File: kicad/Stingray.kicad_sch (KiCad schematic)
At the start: 51 parts, among them J1 Raspberry_Pi_5, J10 USB_A, J11 Screw_Terminal_01x10, J14 Conn_01x04_Pin, J15 USB_A, J16 USB_A, J17 USB_A, J18 USB_A, J19 Screw_Terminal_01x06, J2 Screw_Terminal_01x06, J20 Screw_Terminal_01x06, J3 Conn_01x05_Pin, J4 USB_A, J5 Screw_Terminal_01x06, J6 USB_A, J7 USB_A, J8 USB_A, J9 USB_A, K2 Fujitsu_FTR-LYAA005x, M1 Motor_DC, M2 Motor_DC, Q1 IRLZ44N, Q2 IRLZ44N, Q3 IRLZ44N, SW1 RotaryEncoder, SW2 RotaryEncoder, SW3 E-STOP BUTTON

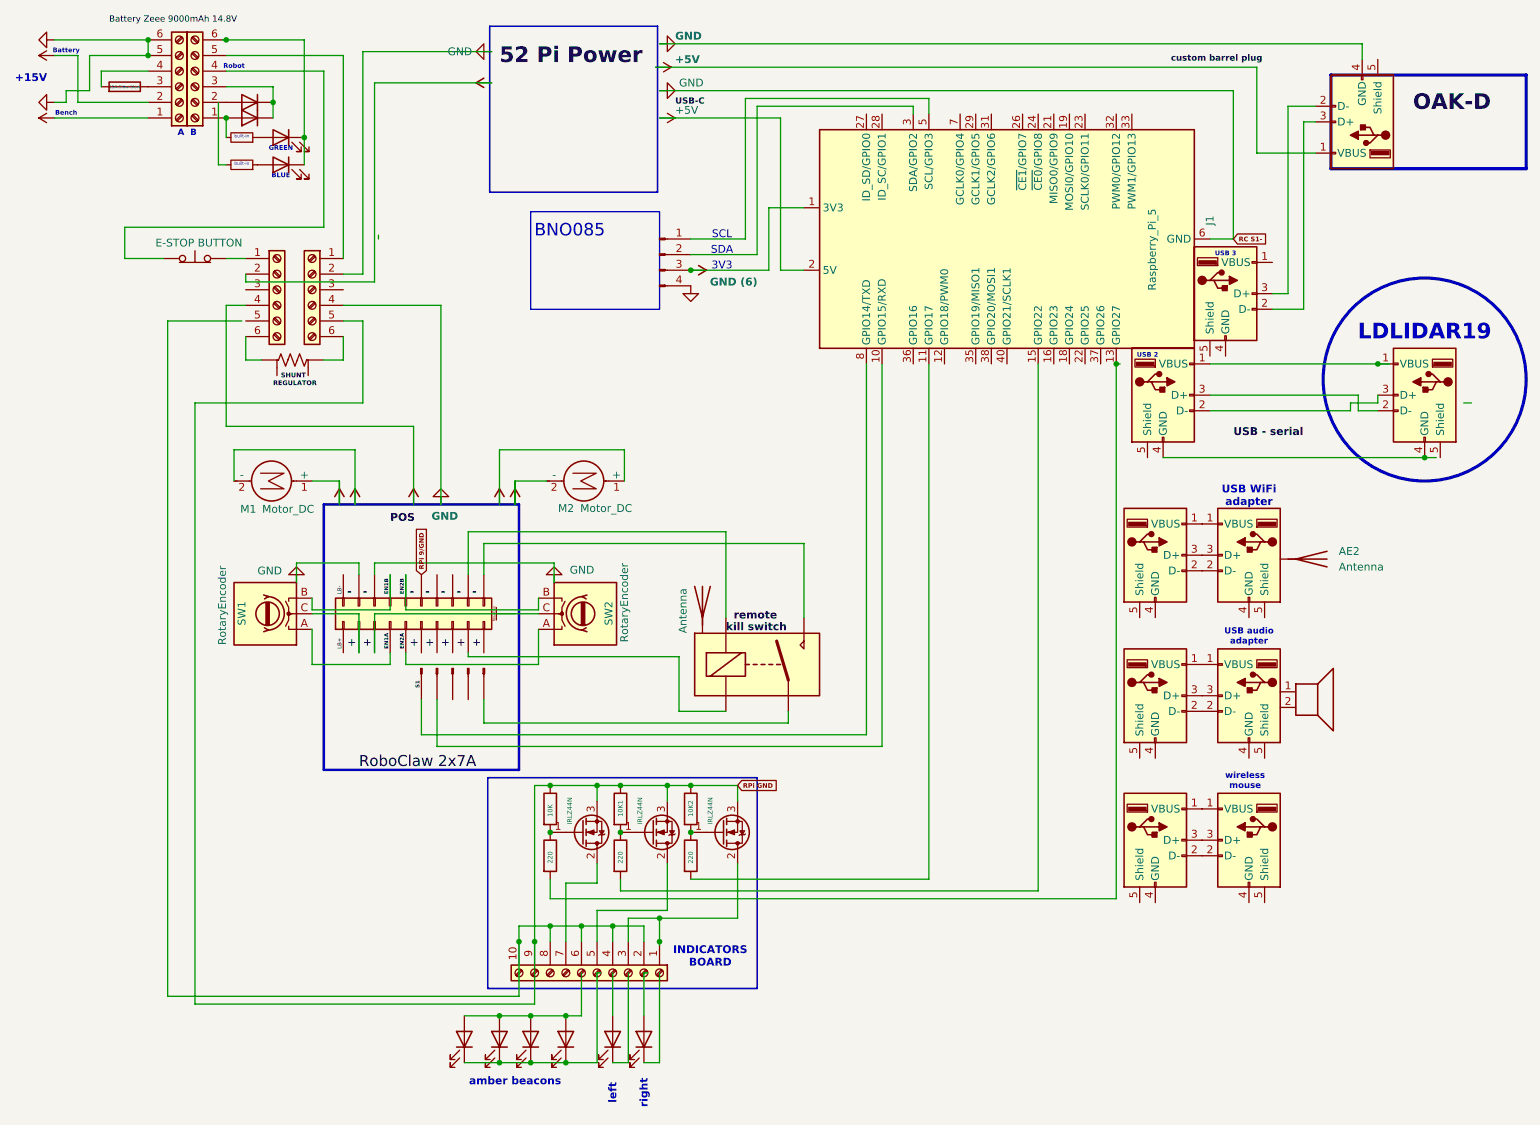
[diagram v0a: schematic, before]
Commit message: kicad: update Stingray schematic - Dual MOSFET power switches
Upload the updated KiCAD source from HankRearden (KiCad 10.0 working copy):
Stingray.kicad_sch reworked with the dual MOSFET high-power switches, plus the
matching Stingray.kicad_pro settings. Matches the new schematic/images already on
main.

Co-authored-by: Copilot <223556219+Copilot@users.noreply.github.com>
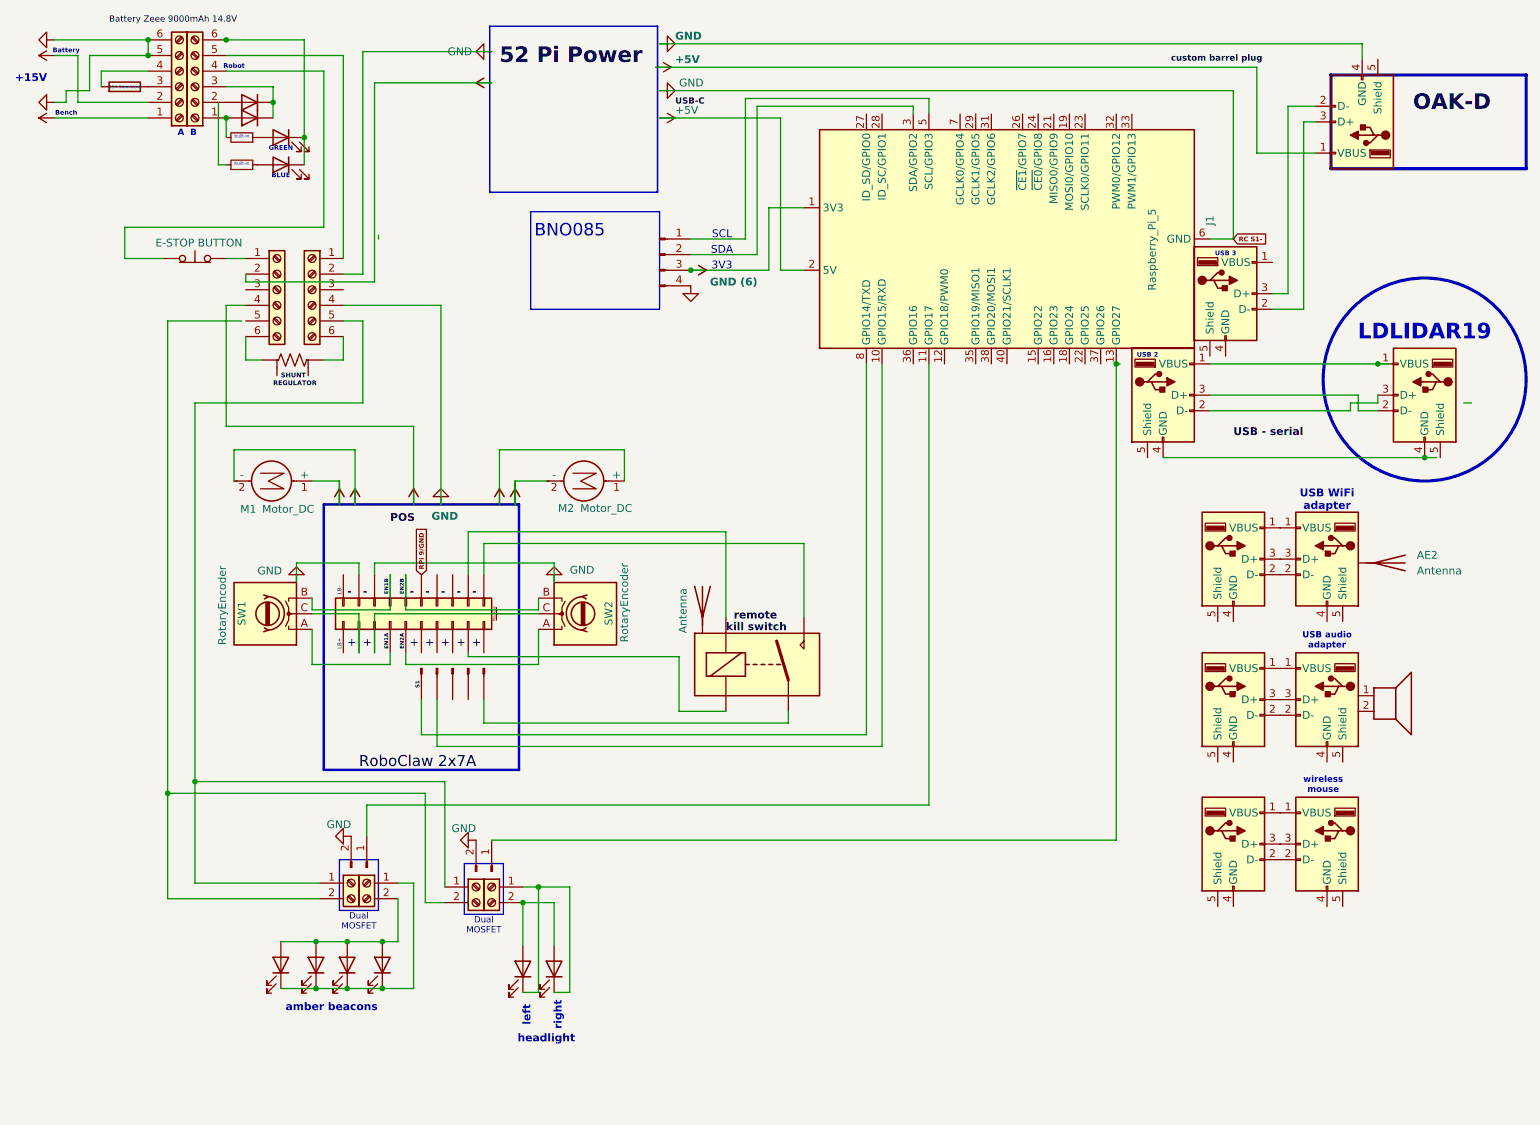
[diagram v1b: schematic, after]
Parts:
- removed 10K, 10K1, 10K2: R, symbol Device:R
- removed J11: Screw_Terminal_01x10, symbol Connector:Screw_Terminal_01x10
- removed Q1, Q2, Q3: IRLZ44N, Package_TO_SOT_THT:TO-220-3_Vertical, symbol Transistor_FET:IRLZ44N
- removed R2, R3, R4: 220, symbol Device:R
- added J11, J12, J21, J23: Screw_Terminal_01x02, symbol Connector:Screw_Terminal_01x02
- added J13, J22: Conn_01x02_Pin, symbol Connector:Conn_01x02_Pin
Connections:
- net GND: now also J13.2 (Pin_2), J22.2 (Pin_2)
- net at D2.1 (K): now also D1.1 (K), J23.1 (Pin_1)
- net at D2.2 (A): now also D1.2 (A), J23.2 (Pin_2)
- net at D4.1 (K), D5.1 (K), D6.1 (K)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: now also J12.1 (Pin_1)
- net at D4.2 (A), D5.2 (A), D6.2 (A)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: now also J12.2 (Pin_2)
- net at J1.11 (GPIO17): now also J13.1 (Pin_1)
- net at J1.13 (GPIO27): now also J22.1 (Pin_1)
- net RPi GND: no longer names the net of J5.5 (Pin_5)
- net RPi GND: now also J11.1 (Pin_1), J21.1 (Pin_1)
- new net: J11.2 (Pin_2), J21.2 (Pin_2)
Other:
- note added: "Dual MOSFET"
- note added: "headlight"
- note removed: "INDICATORS BOARD"
- moved on the sheet: AE2
